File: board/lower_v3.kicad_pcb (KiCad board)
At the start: 2 copper layers, 43.2 x 64.8 mm, 74 parts, among them J1 To Power Bank, J10 PIN_RING_MOTOR, J11 PIN_PINKY_MOTOR, J12 PIN_PINKY_SPLAY, J13 PIN_RING_SPLAY, J14 PIN_MIDDLE_SPLAY, J15 PIN_INDEX_SPLAY, J16 PIN_THUMB_SPLAY, J2 PIN_PINKY, J3 PIN_RING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

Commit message: Finalize board
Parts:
- added J17: PIN_A_BTN, Connector_PinHeader_2.54mm:PinHeader_1x02_P2.54mm_Vertical, F.Cu at (137.2, 129.5)
- added J18: PIN_B_BTN, Connector_PinHeader_2.54mm:PinHeader_1x02_P2.54mm_Vertical, F.Cu at (141.0, 129.5)
- added J19: JOYSTICK, Connector_PinHeader_2.54mm:PinHeader_1x05_P2.54mm_Vertical, F.Cu at (144.1, 135.9)
- moved J15 7.62 mm to (148.6, 95.2)
- moved J16 7.62 mm to (148.6, 91.4)
- moved J3 7.62 mm to (148.6, 123.2)
- moved J4 7.62 mm to (148.6, 119.4)
- moved J5 7.62 mm to (148.6, 115.6)
- moved J12 7.62 mm to (148.6, 106.7)
- moved J13 7.62 mm to (148.6, 102.9)
- moved J14 7.62 mm to (148.6, 99.2)
- moved J2 7.62 mm to (148.6, 127.0)
- moved J6 7.62 mm to (148.6, 111.8)
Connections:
- 83 pad 10: GND -> (no net)
- 83 pad 10: (no net) -> 5V
- 83 pad 10: (no net) -> GND
- 84 pad 10: (no net) -> 3V3
- 84 pad 10: 3V3 -> (no net)
- 84 pad 10: 5V -> (no net)
- J10 pad 2: Net-(J1-Pad2) -> 5V
- J11 pad 2: Net-(J1-Pad2) -> 5V
- J12 pad 1: Net-(U1-Pad13) -> Net-(J12-Pad1)
- J12 pad 2: Net-(J2-Pad2) -> 3V3
- J13 pad 1: Net-(U1-Pad14) -> Net-(J13-Pad1)
- J13 pad 2: Net-(J2-Pad2) -> 3V3
- J14 pad 1: Net-(U1-Pad15) -> Net-(J14-Pad1)
- J14 pad 2: Net-(J2-Pad2) -> 3V3
- J15 pad 1: Net-(U1-Pad16) -> Net-(J15-Pad1)
- J15 pad 2: Net-(J2-Pad2) -> 3V3
- J16 pad 1: Net-(U1-Pad17) -> Net-(U1-Pad20)
- J16 pad 2: Net-(J2-Pad2) -> 3V3
- J2 pad 2: Net-(J2-Pad2) -> 3V3
- J3 pad 2: Net-(J2-Pad2) -> 3V3
- J4 pad 2: Net-(J2-Pad2) -> 3V3
- J5 pad 2: Net-(J2-Pad2) -> 3V3
- J6 pad 2: Net-(J2-Pad2) -> 3V3
- J7 pad 2: Net-(J1-Pad2) -> 5V
- J8 pad 2: Net-(J1-Pad2) -> 5V
- J9 pad 2: Net-(J1-Pad2) -> 5V
- U1 pad 15: Net-(U1-Pad15) -> Net-(J12-Pad1)
- U1 pad 16: Net-(U1-Pad16) -> Net-(J13-Pad1)
- U1 pad 17: Net-(U1-Pad17) -> Net-(J14-Pad1)
- U1 pad 18: unconnected-(U1-Pad18) -> Net-(J15-Pad1)
- U1 pad 20: unconnected-(U1-Pad20) -> Net-(U1-Pad20)
- U1 pad 36: unconnected-(U1-Pad36) -> Net-(U1-Pad36)
- U1 pad 39: unconnected-(U1-Pad39) -> Net-(U1-Pad39)
- U1 pad 41: unconnected-(U1-Pad41) -> Net-(U1-Pad41)
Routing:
- net Net-(J2-Pad2): track 93.9 -> 0.00 mm
- net 3V3: track 27.7 -> 96.1 mm
- net Net-(J1-Pad2): track 66.7 -> 0.00 mm
- net Net-(U1-Pad41): track 0.00 -> 39.1 mm
- net Net-(U1-Pad14): track 8.79 -> 39.7 mm
- net Net-(U1-Pad39): track 0.00 -> 27.2 mm
- net 5V: track 24.1 -> 0.00 mm
- net Net-(U1-Pad13): track 10.00 -> 32.9 mm
- net Net-(U1-Pad36): track 0.00 -> 22.3 mm
- net Net-(J4-Pad1): track 15.1 -> 7.46 mm
- net Net-(U1-Pad15): track 7.58 -> 0.00 mm
- net Net-(J2-Pad1): track 17.3 -> 9.76 mm
- net Net-(J12-Pad1): track 0.00 -> 7.46 mm
- net Net-(J5-Pad1): track 13.8 -> 6.77 mm
- net Net-(J3-Pad1): track 16.3 -> 9.47 mm
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- added copper zone on F.Cu, net 5V
- removed copper zone on F.Cu, net GND
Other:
- board text added: "A"
- board text added: "B"
- board text added: "JOYSTICK"
- board text added: "P"
- board text added: "POWER"
- board text added: "T"
- board text added: "|P---- CURL ----T|"
- board text added: "|P---- SPLAY ----T|"
- board text removed: "|----- CURL -----|"
- board text removed: "|----- SPLAY -----|"

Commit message: Submit Rev B for fabrication
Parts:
- added ?: , , F.Cu at (154.9, 76.2)
- added ?: , , F.Cu at (154.9, 132.1)
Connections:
- J19 pad 3: Net-(J1-Pad2) -> 5V

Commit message: Rev C
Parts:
- J1: value To Power Bank -> POWER; footprint Connector_PinHeader_2.54mm:PinHeader_1x03_P2.54mm_Vertical -> Connector_JST:JST_EH_S4B-EH_1x04_P2.50mm_Horizontal
- moved J11 62.8 mm to (147.3, 68.6), turned to 90 degrees
- moved J10 60.2 mm to (147.3, 72.4), turned to 90 degrees
- moved J9 58.0 mm to (147.3, 76.3), turned to 90 degrees
- moved J8 56.3 mm to (147.3, 80.0), turned to 90 degrees
- moved J7 54.9 mm to (147.3, 83.8), turned to 90 degrees
- moved J1 52.3 mm to (124.5, 123.2), turned to 180 degrees
- moved ? 14.5 mm to (141.6, 70.5)
- moved J18 13.7 mm to (129.5, 121.9)
- moved J19 8.55 mm to (148.6, 128.6), turned to -90 degrees
- moved J17 7.94 mm to (134.9, 121.9)
- moved 83 7.73 mm to (127.0, 78.7)
- moved 83 7.73 mm to (127.0, 86.4)
- moved 83 7.73 mm to (127.0, 83.8)
- moved 83 7.73 mm to (127.0, 73.7)
- moved 83 7.73 mm to (127.0, 91.4)
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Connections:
- 83 pad 10: 5V -> /5V
- 84 pad 10: 3V3 -> /3V3
- J1 pad 2: 5V -> /3V3
- J1 pad 3: GND -> /5V
- J10 pad 2: 5V -> /5V
- J11 pad 2: 5V -> /5V
- J12 pad 2: 3V3 -> /3V3
- J13 pad 2: 3V3 -> /3V3
- J14 pad 2: 3V3 -> /3V3
- J15 pad 2: 3V3 -> /3V3
- J16 pad 2: 3V3 -> /3V3
- J17 pad 1: Net-(U1-Pad36) -> Net-(U1-Pad39)
- J18 pad 1: Net-(U1-Pad39) -> Net-(U1-Pad36)
- J19 pad 1: GND -> /3V3
- J19 pad 2: Net-(U1-Pad41) -> Net-(J19-Pad2)
- J19 pad 3: 5V -> Net-(U1-Pad41)
- J19 pad 4: Net-(U1-Pad13) -> GND
- J19 pad 5: Net-(U1-Pad14) -> Net-(J19-Pad5)
- J2 pad 2: 3V3 -> /3V3
- J3 pad 2: 3V3 -> /3V3
- J4 pad 2: 3V3 -> /3V3
- J5 pad 2: 3V3 -> /3V3
- J6 pad 2: 3V3 -> /3V3
- J7 pad 2: 5V -> /5V
- J8 pad 2: 5V -> /5V
- J9 pad 2: 5V -> /5V
- U1 pad 103: 5V -> /5V
- U1 pad 104: 3V3 -> unconnected-(U1-Pad104)
- U1 pad 13: Net-(U1-Pad13) -> Net-(J19-Pad5)
- U1 pad 14: Net-(U1-Pad14) -> Net-(J19-Pad2)
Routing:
- net /3V3: track 0.00 -> 103.5 mm
- net 3V3: track 96.1 -> 0.00 mm
- net Net-(U1-Pad14): track 39.7 -> 0.00 mm
- net Net-(J19-Pad2): track 0.00 -> 35.0 mm
- net Net-(U1-Pad13): track 32.9 -> 0.00 mm
- net Net-(J8-Pad1): track 19.1 -> 51.7 mm
- net Net-(J19-Pad5): track 0.00 -> 32.5 mm
- net Net-(J7-Pad1): track 28.9 -> 58.2 mm
- net Net-(J9-Pad1): track 23.2 -> 49.4 mm
- net Net-(J10-Pad1): track 27.3 -> 49.6 mm
- net Net-(J11-Pad1): track 31.5 -> 50.5 mm
- net Net-(U1-Pad36): track 22.3 -> 16.0 mm
- net Net-(U1-Pad39): track 27.2 -> 22.4 mm
- net Net-(J4-Pad1): track 7.46 -> 11.9 mm
- net Net-(U1-Pad15): track 7.46 -> 11.9 mm
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- added copper zone on F.Cu, net /5V
- removed copper zone on F.Cu, net 5V
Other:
- board text added: "ClearGauntlet Rev.C"
- board text added: "|T---- SERVO ----P|"
- board text removed: "ClearGauntlet Rev.B"
- board text removed: "P"
- board text removed: "T"
- board text removed: "|-MOTOR-|"

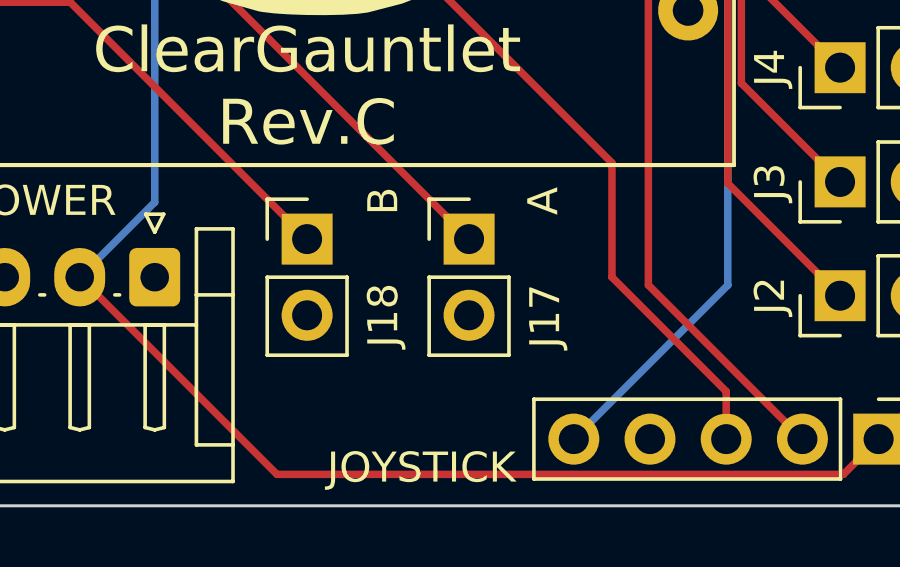
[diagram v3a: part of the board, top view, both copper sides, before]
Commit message: Locate OpAmp and Photo Diodes
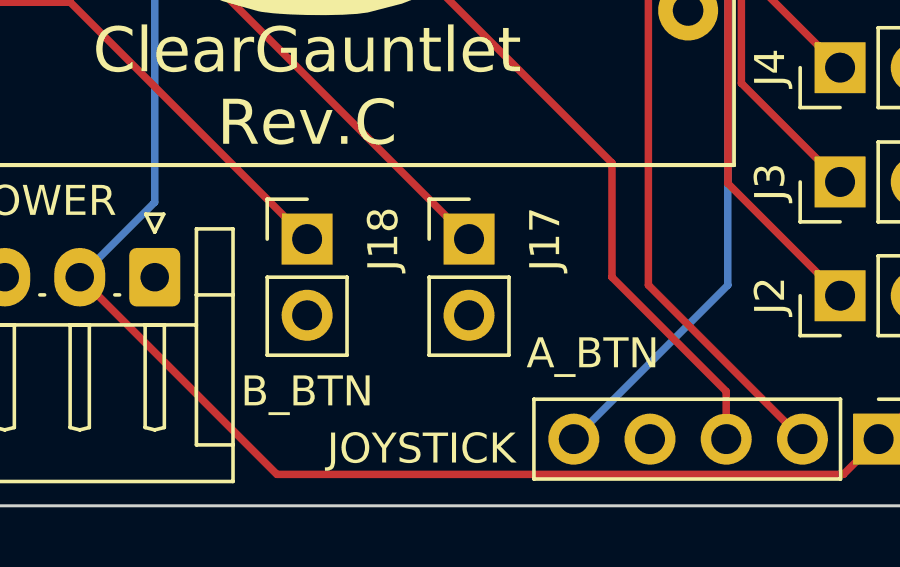
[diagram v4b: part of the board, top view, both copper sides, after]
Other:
- board text added: "A_BTN"
- board text added: "B_BTN"
- board text removed: "A"
- board text removed: "B"
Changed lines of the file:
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@@
     (property "Sheetname" "")
     (attr through_hole)
-    (fp_text reference "J18" (at 2.54 2.54 270) (layer "F.SilkS")
+    (fp_text reference "J18" (at 2.54 0 270) (layer "F.SilkS")
       (effects (font (size 1 1) (thickness 0.15)))
     )
@@
     (property "Sheetname" "")
     (attr through_hole)
-    (fp_text reference "J17" (at 2.54 2.57 270) (layer "F.SilkS")
+    (fp_text reference "J17" (at 2.54 0 270) (layer "F.SilkS")
       (effects (font (size 1 1) (thickness 0.15)))
     )
@@
     (effects (font (size 1 1) (thickness 0.15)))
   )
-  (gr_text "JOYSTICK" (at 133.35 129.54) (layer "F.SilkS")
+  (gr_text "JOYSTICK" (at 133.35 128.905) (layer "F.SilkS")
     (effects (font (size 1 1) (thickness 0.15)))
   )
-  (gr_text "A" (at 137.414 120.65 90) (layer "F.SilkS")
+  (gr_text "A_BTN" (at 139.065 125.73) (layer "F.SilkS")
     (effects (font (size 1 1) (thickness 0.15)))
   )
@@
     (effects (font (size 1 1) (thickness 0.15)))
   )
-  (gr_text "B" (at 132.08 120.65 90) (layer "F.SilkS")
+  (gr_text "B_BTN" (at 129.54 127) (layer "F.SilkS")
     (effects (font (size 1 1) (thickness 0.15)))
   )
@@
     (effects (font (size 1 1) (thickness 0.15)))
   )
+  (gr_text "5V" (at 119.38 131.445 270) (layer "Cmts.User")
+    (effects (font (size 1 1) (thickness 0.15)) (justify left))
+  )
+  (gr_text "GND	" (at 124.46 131.445 270) (layer "Cmts.User")
+    (effects (font (size 1 1) (thickness 0.15)) (justify left))
+  )
+  (gr_text "3V3" (at 121.92 131.445 270) (layer "Cmts.User")
+    (effects (font (size 1 1) (thickness 0.15)) (justify left))
+  )
+  (gr_text "GND	" (at 116.84 131.445 270) (layer "Cmts.User")
+    (effects (font (size 1 1) (thickness 0.15)) (justify left))
+  )
   (segment (start 143.565 120.0675) (end 143.565 113.085) (width 0.25) (layer "F.Cu") (net 3))

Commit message: RevC RC 1
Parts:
- removed 83 (x24), 84 (x32), ? (x2): , 
- removed J17: PIN_A_BTN, Connector_PinHeader_2.54mm:PinHeader_1x02_P2.54mm_Vertical
- removed J18: PIN_B_BTN, Connector_PinHeader_2.54mm:PinHeader_1x02_P2.54mm_Vertical
- removed logo: LOGO, CG:logo-big
- added C1: C_Polarized, Capacitor_THT:CP_Radial_D10.0mm_P5.00mm, F.Cu at (122.2, 96.5)
- added G***: LOGO, cg_logo_small:cg_logo_med, F.Cu at (129.8, 110.2)
- added R1: R_US, Resistor_THT:R_Axial_DIN0309_L9.0mm_D3.2mm_P12.70mm_Horizontal, F.Cu at (132.7, 81.3)
- J1: footprint Connector_JST:JST_EH_S4B-EH_1x04_P2.50mm_Horizontal -> Connector_JST:JST_EH_B4B-EH-A_1x04_P2.50mm_Vertical
- J19: value JOYSTICK -> Conn_01x08_Male; footprint Connector_PinHeader_2.54mm:PinHeader_1x05_P2.54mm_Vertical -> Connector_PinSocket_2.54mm:PinSocket_2x04_P2.54mm_Vertical
- moved J19 62.3 mm to (134.6, 67.9), turned to 90 degrees
- moved J1 55.3 mm to (118.2, 68.3), turned to 0 degrees
- moved J7 15.9 mm to (146.1, 68.0)
- moved J11 15.0 mm to (146.1, 83.6)
- moved J8 8.25 mm to (146.1, 71.9)
- moved J10 7.38 mm to (146.1, 79.7)
- moved U1 4.44 mm to (129.5, 98.4)
- moved J6 2.06 mm to (146.1, 106.9)
- moved J5 2.00 mm to (146.1, 110.8)
- moved J4 1.93 mm to (146.1, 114.7)
- moved J3 1.86 mm to (146.1, 118.6)
- moved J2 1.79 mm to (146.1, 122.5)
- moved J16 1.49 mm to (146.1, 87.5)
- moved J14 1.46 mm to (146.1, 95.3)
- moved J15 1.45 mm to (146.1, 91.4)
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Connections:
- J10 pad 1: Net-(J10-Pad1) -> Net-(U1-Pad25)
- J12 pad 1: Net-(U1-Pad15) -> Net-(J12-Pad1)
- J13 pad 1: Net-(U1-Pad16) -> Net-(J13-Pad1)
- J14 pad 1: Net-(U1-Pad17) -> Net-(J14-Pad1)
- J16 pad 1: /Net-(U1-Pad20) -> Net-(J16-Pad1)
- J19 pad 3: Net-(U1-Pad41) -> Net-(J19-Pad3)
- J7 pad 1: Net-(J7-Pad1) -> Net-(U1-Pad21)
- J8 pad 1: Net-(J8-Pad1) -> Net-(U1-Pad22)
- J9 pad 1: Net-(J9-Pad1) -> Net-(U1-Pad24)
- U1 pad 102: GND -> unconnected-(U1-Pad102)
- U1 pad 103: /5V -> unconnected-(U1-Pad103)
- U1 pad 104: unconnected-(U1-Pad104) -> /3V3
- U1 pad 13: Net-(J19-Pad5) -> Net-(J12-Pad1)
- U1 pad 14: Net-(J19-Pad2) -> Net-(J13-Pad1)
- U1 pad 15: Net-(U1-Pad15) -> Net-(J14-Pad1)
- U1 pad 16: Net-(U1-Pad16) -> Net-(J15-Pad1)
- U1 pad 17: Net-(U1-Pad17) -> Net-(J16-Pad1)
- U1 pad 18: Net-(J15-Pad1) -> unconnected-(U1-Pad18)
- U1 pad 21: unconnected-(U1-Pad21) -> Net-(U1-Pad21)
- U1 pad 22: unconnected-(U1-Pad22) -> Net-(U1-Pad22)
- U1 pad 24: unconnected-(U1-Pad24) -> Net-(U1-Pad24)
- U1 pad 25: unconnected-(U1-Pad25) -> Net-(U1-Pad25)
- U1 pad 27: Net-(J7-Pad1) -> Net-(J11-Pad1)
- U1 pad 34: Net-(J11-Pad1) -> unconnected-(U1-Pad34)
- U1 pad 35: Net-(J10-Pad1) -> unconnected-(U1-Pad35)
- U1 pad 36: Net-(U1-Pad36) -> Net-(J19-Pad8)
- U1 pad 38: Net-(J9-Pad1) -> Net-(J19-Pad6)
- U1 pad 39: Net-(U1-Pad39) -> Net-(J19-Pad7)
- U1 pad 40: unconnected-(U1-Pad40) -> Net-(J19-Pad3)
- U1 pad 41: Net-(U1-Pad41) -> Net-(J19-Pad2)
- U1 pad 42: Net-(J8-Pad1) -> Net-(J19-Pad5)
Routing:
- net Net-(J19-Pad7): track 0.00 -> 59.9 mm
- net Net-(J19-Pad8): track 0.00 -> 58.5 mm
- net Net-(J7-Pad1): track 58.2 -> 0.00 mm
- net Net-(J19-Pad3): track 0.00 -> 57.8 mm
- net Net-(J19-Pad6): track 0.00 -> 54.0 mm, vias 0 -> 1
- net Net-(J8-Pad1): track 51.7 -> 0.00 mm
- net Net-(J10-Pad1): track 49.6 -> 0.00 mm
- net Net-(J9-Pad1): track 49.4 -> 0.00 mm
- net Net-(U1-Pad21): track 0.00 -> 44.8 mm
- net Net-(U1-Pad22): track 0.00 -> 42.3 mm
- net Net-(U1-Pad25): track 0.00 -> 41.6 mm
- net Net-(U1-Pad24): track 0.00 -> 40.3 mm
- net Net-(U1-Pad41): track 38.0 -> 0.00 mm
- net Net-(J19-Pad5): track 32.5 -> 58.7 mm, vias 0 -> 1
- net Net-(U1-Pad39): track 22.4 -> 0.00 mm
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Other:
- board size 43.2 x 64.8 mm -> 39.6 x 59.9 mm
- board text added: "Bruh."
- board text added: "|P---- SERVO ----T|"
- board text removed: "A_BTN"
- board text removed: "B_BTN"
- board text removed: "|T---- SERVO ----P|"

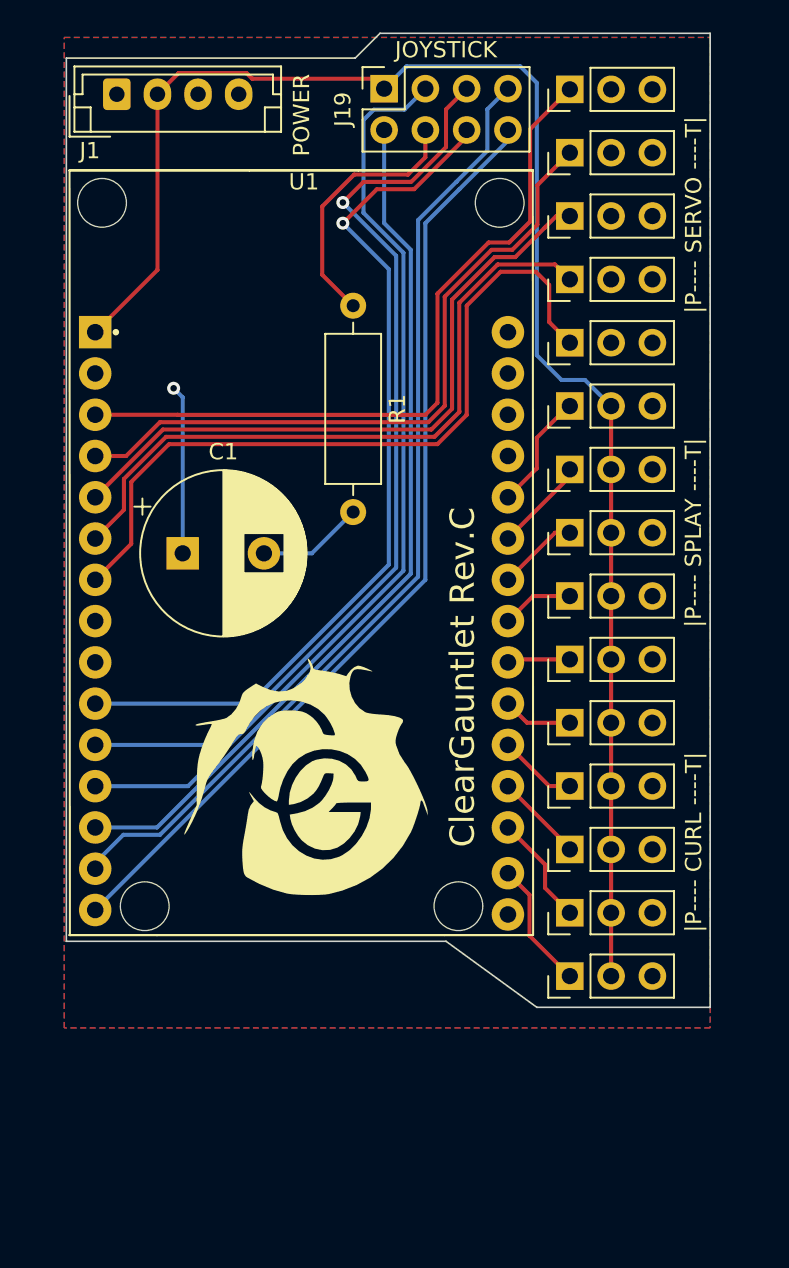
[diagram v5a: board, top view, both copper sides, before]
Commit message: Rev C RC 1.1
Oops wanted to make absolutely sure the ground and 5V planes were
properly connected
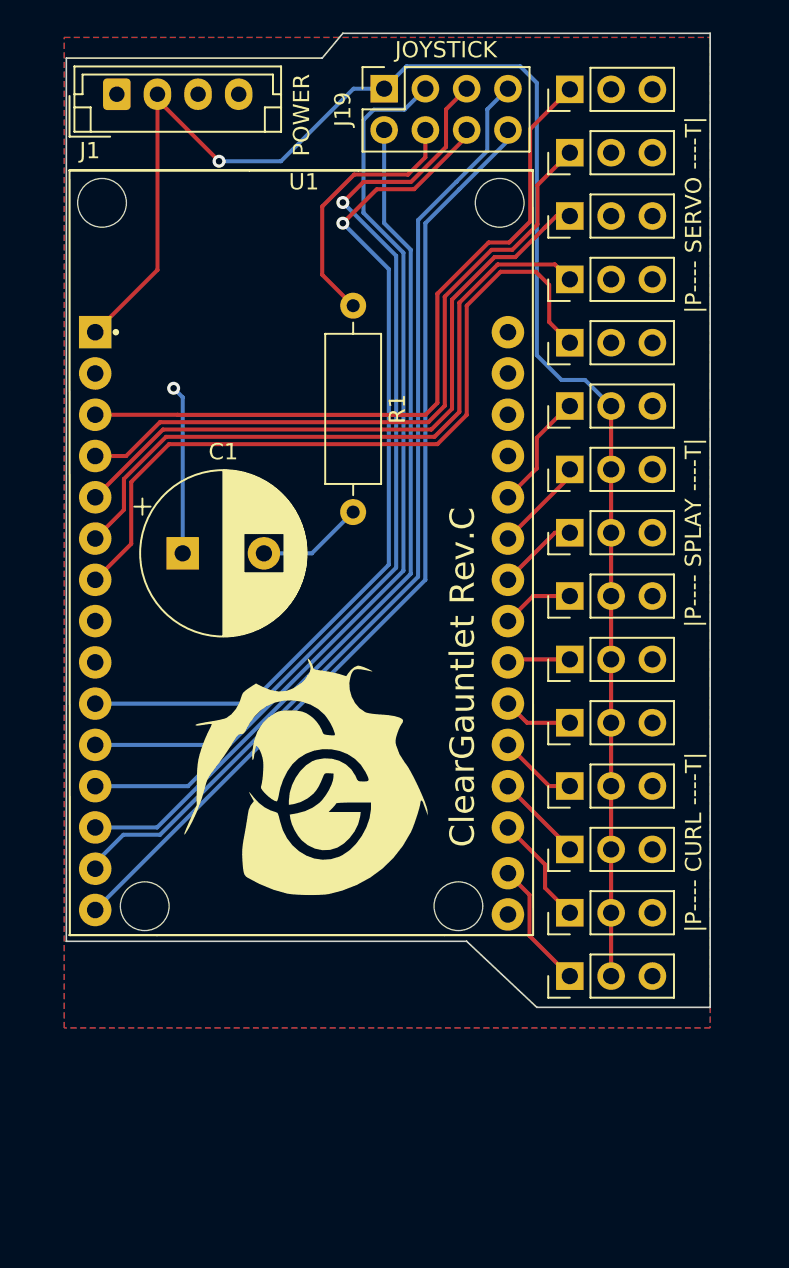
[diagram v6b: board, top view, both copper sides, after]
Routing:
- net /3V3: track 98.9 -> 102.6 mm, vias 0 -> 1
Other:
- outline, holes or cut-outs redrawn
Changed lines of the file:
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@@
     )
     (model "${KIPRJMOD}/3rdparty/ESP32-DEVKIT-V1/ESP-32_v1.STEP"
-      (offset (xyz -6.6 -6.6 -43))
+      (offset (xyz -6.4 -6.3 -42.5))
       (scale (xyz 1 1 1))
       (rotate (xyz 0 0 180))
@@
       (net 26 "Net-(C1-Pad2)") (pintype "passive"))
     (model "${KICAD6_3DMODEL_DIR}/Capacitor_THT.3dshapes/CP_Radial_D10.0mm_P5.00mm.wrl"
-      (offset (xyz 0 0 0))
-      (scale (xyz 1 1 1))
-      (rotate (xyz 0 0 0))
+      (offset (xyz 0 0 5.1))
+      (scale (xyz 1 1 1))
+      (rotate (xyz 90 0 0))
     )
   )
@@
       (xy 154.686 124.46)
       (xy 144.018 124.46)
-      (xy 138.43 120.396)
+      (xy 139.7 120.396)
       (xy 115.062 120.396)
       (xy 115.062 66.04)
-      (xy 132.842 66.04)
-      (xy 134.366 64.516)
+      (xy 130.81 66.04)
+      (xy 132.08 64.516)
       (xy 154.686 64.516)
     ) (layer "Edge.Cuts") (width 0.1) (fill none))
@@
   (segment (start 146.05 91.8) (end 142.24 95.61) (width 0.25) (layer "F.Cu") (net 9))
   (segment (start 146.05 91.35321) (end 146.05 91.8) (width 0.25) (layer "F.Cu") (net 9))
-  (segment (start 126.156701 66.965) (end 121.97 66.965) (width 0.25) (layer "F.Cu") (net 10))
+  (segment (start 120.67 68.265) (end 120.67 68.6) (width 0.25) (layer "F.Cu") (net 10))
   (segment (start 134.62 67.925) (end 134.005 67.31) (width 0.25) (layer "F.Cu") (net 10))
-  (segment (start 121.97 66.965) (end 120.67 68.265) (width 0.25) (layer "F.Cu") (net 10))
   (segment (start 148.59 87.455175) (end 148.59 122.5375) (width 0.25) (layer "F.Cu") (net 10))
-  (segment (start 134.005 67.31) (end 126.501701 67.31) (width 0.25) (layer "F.Cu") (net 10))
+  (segment (start 120.67 68.6) (end 124.46 72.39) (width 0.25) (layer "F.Cu") (net 10))
   (segment (start 116.84 82.91) (end 120.67 79.08) (width 0.25) (layer "F.Cu") (net 10))
   (segment (start 120.67 79.08) (end 120.67 68.6) (width 0.25) (layer "F.Cu") (net 10))
-  (segment (start 126.501701 67.31) (end 126.156701 66.965) (width 0.25) (layer "F.Cu") (net 10))
+  (via (at 124.46 72.39) (size 0.8) (drill 0.4) (layers "F.Cu" "B.Cu") (free) (net 10))
   (segment (start 144.018 67.564) (end 144.018 84.328) (width 0.25) (layer "B.Cu") (net 10))
   (segment (start 146.986825 85.852) (end 148.59 87.455175) (width 0.25) (layer "B.Cu") (net 10))
   (segment (start 135.997 66.548) (end 134.62 67.925) (width 0.25) (layer "B.Cu") (net 10))
+  (segment (start 132.735 67.925) (end 128.27 72.39) (width 0.25) (layer "B.Cu") (net 10))
   (segment (start 135.997 66.548) (end 143.002 66.548) (width 0.25) (layer "B.Cu") (net 10))
+  (segment (start 134.62 67.925) (end 132.735 67.925) (width 0.25) (layer "B.Cu") (net 10))
   (segment (start 144.018 84.328) (end 145.542 85.852) (width 0.25) (layer "B.Cu") (net 10))
   (segment (start 143.002 66.548) (end 144.018 67.564) (width 0.25) (layer "B.Cu") (net 10))
+  (segment (start 128.27 72.39) (end 124.46 72.39) (width 0.25) (layer "B.Cu") (net 10))
   (segment (start 145.542 85.852) (end 146.986825 85.852) (width 0.25) (layer "B.Cu") (net 10))
   (via (at 121.666 86.36) (size 0.8) (drill 0.4) (layers "F.Cu" "B.Cu") (free) (net 11))

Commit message: Smallerize resistor
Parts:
- R1: footprint Resistor_THT:R_Axial_DIN0309_L9.0mm_D3.2mm_P12.70mm_Horizontal -> Resistor_THT:R_Axial_DIN0207_L6.3mm_D2.5mm_P10.16mm_Horizontal
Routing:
- net Net-(C1-Pad2): track 6.54 -> 9.08 mm
- net /3V3: track 102.6 -> 101.7 mm

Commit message: Fix Joystick port pin layout
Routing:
- net GND: track 16.2 -> 0.00 mm
- net Net-(J19-Pad5): track 58.7 -> 52.4 mm
- net Net-(J19-Pad7): track 59.9 -> 56.3 mm
- net Net-(J19-Pad2): track 53.9 -> 57.1 mm
- net Net-(J19-Pad6): track 54.0 -> 51.6 mm
- net /3V3: track 101.7 -> 101.0 mm
- net Net-(J19-Pad3): track 57.8 -> 57.4 mm, vias 0 -> 1
